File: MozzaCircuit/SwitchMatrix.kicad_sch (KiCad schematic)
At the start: 94 parts, among them SW13 SW_ChocV2_rev, SW14 SW_ChocV2_rev, SW15 SW_ChocV2_rev, SW21 SW_ChocV2_rev, SW22 SW_ChocV2_rev, SW23 SW_ChocV2_rev, SW24 SW_ChocV2_rev, SW25 SW_ChocV2_rev, SW31 SW_ChocV2_rev, SW32 SW_ChocV2_rev, SW33 SW_ChocV2_rev, SW34 SW_ChocV2_rev, SW35 SW_ChocV2_rev, SW41 SW_ChocV2_rev, SW42 SW_ChocV2_rev, SW43 SW_ChocV2_rev, SW44 SW_ChocV2_rev, SW51 SW_ChocV2_rev, SW52 SW_ChocV2_rev, SW53 SW_ChocV2_rev, SW54 SW_ChocV2_rev, SW61 SW_ChocV2_rev, SW62 SW_ChocV2_rev, SW63 SW_ChocV2_rev, SW64 SW_ChocV2_rev, SW71 SW_ChocV2_rev, SW72 SW_ChocV2_rev, SW73 SW_ChocV2_rev, SW82 SW_ChocV2_rev, SW83 SW_ChocV2_rev, SW84 SW_ChocV2_rev

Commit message: led right ends wiring
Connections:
- net 5VD: now also SW25.4; no longer SW25.5
- net GNDD: now also SW25.5; no longer SW25.4
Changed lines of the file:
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@@
   (junction (at 160.02 91.44) (diameter 0) (color 0 0 0 0)
   )
+  (junction (at 72.39 138.43) (diameter 0) (color 0 0 0 0)
+  )
   (junction (at 50.8 76.2) (diameter 0) (color 0 0 0 0)
   )
@@
   (junction (at 234.95 138.43) (diameter 0) (color 0 0 0 0)
   )
+  (junction (at 72.39 130.81) (diameter 0) (color 0 0 0 0)
+  )
   (junction (at 129.54 113.03) (diameter 0) (color 0 0 0 0)
   )
@@
   (junction (at 91.44 80.01) (diameter 0) (color 0 0 0 0)
   )
+  (junction (at 53.34 130.81) (diameter 0) (color 0 0 0 0)
+  )
   (junction (at 88.9 160.02) (diameter 0) (color 0 0 0 0)
   )
@@
   (junction (at 64.77 116.84) (diameter 0) (color 0 0 0 0)
   )
+  (junction (at 53.34 138.43) (diameter 0) (color 0 0 0 0)
+  )
   (junction (at 146.05 160.02) (diameter 0) (color 0 0 0 0)
   )
@@
     (stroke (width 0) (type default) (color 0 0 0 0))
   )
+  (wire (pts (xy 34.29 130.81) (xy 53.34 130.81))
+    (stroke (width 0) (type default) (color 0 0 0 0))
+  )
   (wire (pts (xy 110.49 80.01) (xy 129.54 80.01))
     (stroke (width 0) (type default) (color 0 0 0 0))
@@
     (stroke (width 0) (type default) (color 0 0 0 0))
   )
+  (wire (pts (xy 34.29 138.43) (xy 53.34 138.43))
+    (stroke (width 0) (type default) (color 0 0 0 0))
+  )
   (wire (pts (xy 165.1 154.94) (xy 184.15 154.94))
     (stroke (width 0) (type default) (color 0 0 0 0))
@@
     (stroke (width 0) (type default) (color 0 0 0 0))
   )
+  (wire (pts (xy 53.34 138.43) (xy 72.39 138.43))
+    (stroke (width 0) (type default) (color 0 0 0 0))
+  )
   (wire (pts (xy 53.34 105.41) (xy 72.39 105.41))
     (stroke (width 0) (type default) (color 0 0 0 0))
@@
   )
   (wire (pts (xy 72.39 138.43) (xy 184.15 138.43))
+    (stroke (width 0) (type default) (color 0 0 0 0))
+  )
+  (wire (pts (xy 53.34 130.81) (xy 72.39 130.81))
     (stroke (width 0) (type default) (color 0 0 0 0))
   )
@@
     )
   )
-  (global_label "5VD" (shape input) (at 53.34 138.43 0) (fields_autoplaced)
-    (effects (font (size 1.27 1.27)) (justify left))
-    (property "Intersheet References" "${INTERSHEET_REFS}" (id 0) (at 59.3212 138.3506 0)
-      (effects (font (size 1.27 1.27)) (justify left) hide)
-    )
-  )
   (global_label "COL7" (shape input) (at 146.05 167.64 270) (fields_autoplaced)
     (effects (font (size 1.27 1.27)) (justify right))
@@
     (effects (font (size 1.27 1.27)) (justify left))
     (property "Intersheet References" "${INTERSHEET_REFS}" (id 0) (at 191.8245 101.5206 0)
-      (effects (font (size 1.27 1.27)) (justify left) hide)
-    )
-  )
-  (global_label "5VD" (shape input) (at 34.29 130.81 0) (fields_autoplaced)
-    (effects (font (size 1.27 1.27)) (justify left))
-    (property "Intersheet References" "${INTERSHEET_REFS}" (id 0) (at 40.2712 130.7306 0)
       (effects (font (size 1.27 1.27)) (justify left) hide)
     )
@@
     (pin "2")
   )
-  (symbol (lib_id "power:GNDD") (at 53.34 130.81 90) (unit 1)
-    (in_bom yes) (on_board yes) (fields_autoplaced)
-    (property "Reference" "#PWR0138" (id 0) (at 59.69 130.81 0)
-      (effects (font (size 1.27 1.27)) hide)
-    )
-    (property "Value" "GNDD" (id 1) (at 57.15 130.8099 90)
-      (effects (font (size 1.27 1.27)) (justify right))
-    )
-    (property "Footprint" "" (id 2) (at 53.34 130.81 0)
-      (effects (font (size 1.27 1.27)) hide)
-    )
-    (property "Datasheet" "" (id 3) (at 53.34 130.81 0)
-      (effects (font (size 1.27 1.27)) hide)
-    )
-    (pin "1")
-  )
   (symbol (lib_id "Device:D_Small") (at 86.36 91.44 0) (unit 1)
     (in_bom yes) (on_board yes)
@@
     (pin "5")
   )
-  (symbol (lib_id "power:GNDD") (at 34.29 138.43 90) (unit 1)
-    (in_bom yes) (on_board yes) (fields_autoplaced)
-    (property "Reference" "#PWR0139" (id 0) (at 40.64 138.43 0)
-      (effects (font (size 1.27 1.27)) hide)
-    )
-    (property "Value" "GNDD" (id 1) (at 38.1 138.4299 90)
-      (effects (font (size 1.27 1.27)) (justify right))
-    )
-    (property "Footprint" "" (id 2) (at 34.29 138.43 0)
-      (effects (font (size 1.27 1.27)) hide)
-    )
-    (property "Datasheet" "" (id 3) (at 34.29 138.43 0)
-      (effects (font (size 1.27 1.27)) hide)
-    )
-    (pin "1")
-  )
   (symbol (lib_name "SW_ChocV2_rev_12") (lib_id "00_KeyParts:SW_ChocV2_rev") (at 69.85 83.82 90) (mirror x) (unit 1)

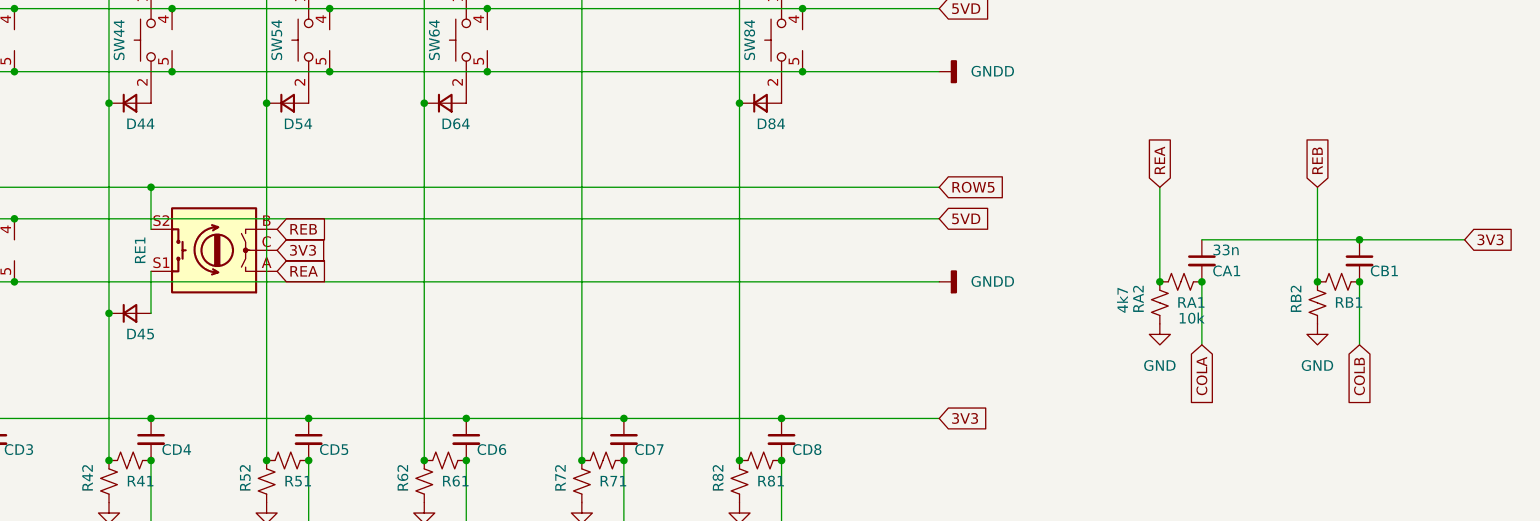
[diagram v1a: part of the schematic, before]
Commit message: rotend debounce
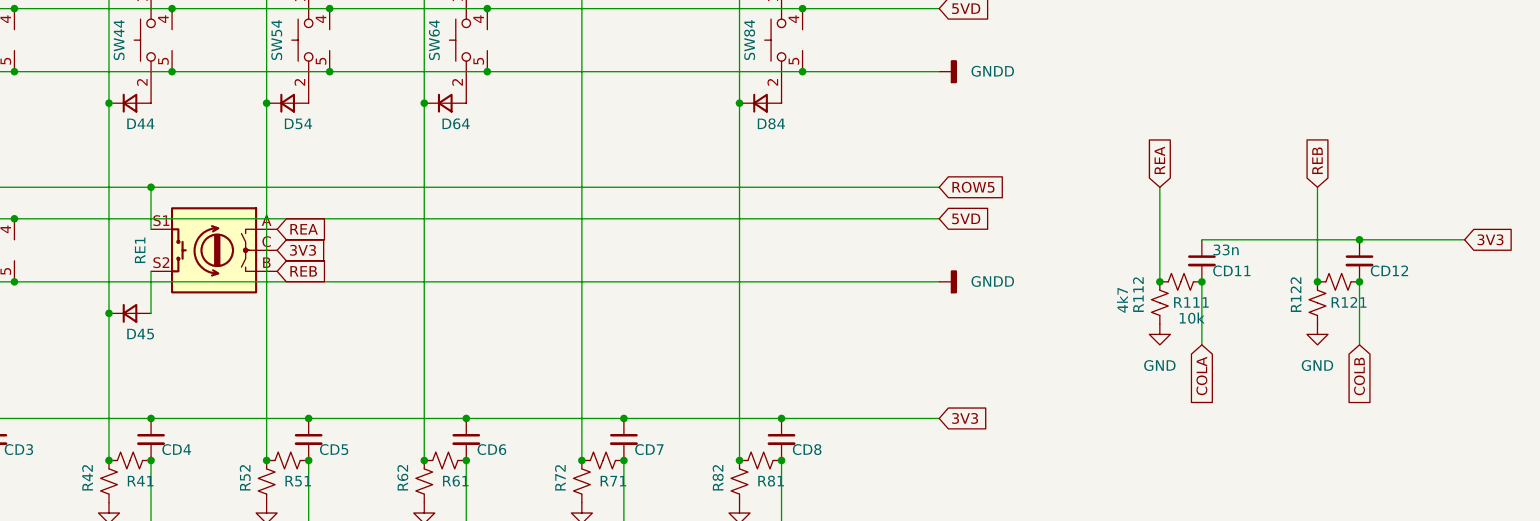
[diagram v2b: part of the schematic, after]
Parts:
- renumbered CA1 to CD11, CB1 to CD12, RA1 to R111, RA2 to R112, RB1 to R121, RB2 to R122
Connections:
- net ROW5: now also RE1.S1; no longer RE1.S2
- net at D45.2 (A): now also RE1.S2; no longer RE1.S1
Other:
- moved on the sheet: RE1
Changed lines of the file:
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@@
     )
   )
-  (global_label "REA" (shape input) (at 104.14 137.16 0) (fields_autoplaced)
+  (global_label "REA" (shape input) (at 104.14 132.08 0) (fields_autoplaced)
     (effects (font (size 1.27 1.27)) (justify left))
-    (property "Intersheet References" "${INTERSHEET_REFS}" (id 0) (at 110.0607 137.0806 0)
+    (property "Intersheet References" "${INTERSHEET_REFS}" (id 0) (at 110.0607 132.0006 0)
       (effects (font (size 1.27 1.27)) (justify left) hide)
     )
@@
     )
   )
-  (global_label "REB" (shape input) (at 104.14 132.08 0) (fields_autoplaced)
+  (global_label "REB" (shape input) (at 104.14 137.16 0) (fields_autoplaced)
     (effects (font (size 1.27 1.27)) (justify left))
-    (property "Intersheet References" "${INTERSHEET_REFS}" (id 0) (at 110.2421 132.0006 0)
+    (property "Intersheet References" "${INTERSHEET_REFS}" (id 0) (at 110.2421 137.0806 0)
       (effects (font (size 1.27 1.27)) (justify left) hide)
     )
@@
   (symbol (lib_id "Device:C_Small") (at 215.9 135.89 0) (unit 1)
     (in_bom yes) (on_board yes)
-    (property "Reference" "CA1" (id 0) (at 217.17 137.16 0)
+    (property "Reference" "CD11" (id 0) (at 217.17 137.16 0)
       (effects (font (size 1.27 1.27)) (justify left))
     )
@@
   (symbol (lib_id "Device:R_Small_US") (at 232.41 138.43 90) (unit 1)
     (in_bom yes) (on_board yes)
-    (property "Reference" "RB1" (id 0) (at 233.68 140.97 90))
+    (property "Reference" "R121" (id 0) (at 233.68 140.97 90))
     (property "Value" "R_Small_US" (id 1) (at 232.41 134.62 90)
       (effects (font (size 1.27 1.27)) hide)
@@
   (symbol (lib_id "Device:R_Small_US") (at 210.82 140.97 0) (unit 1)
     (in_bom yes) (on_board yes)
-    (property "Reference" "RA2" (id 0) (at 208.28 142.24 90)
+    (property "Reference" "R112" (id 0) (at 208.28 142.24 90)
       (effects (font (size 1.27 1.27)) (justify left))
     )
@@
     (pin "1")
   )
-  (symbol (lib_id "Device:RotaryEncoder_Switch") (at 96.52 134.62 180) (unit 1)
+  (symbol (lib_id "Device:RotaryEncoder_Switch") (at 96.52 134.62 0) (mirror y) (unit 1)
     (in_bom yes) (on_board yes)
     (property "Reference" "RE1" (id 0) (at 87.63 134.62 90))
-    (property "Value" "RotaryEncoder_Switch" (id 1) (at 96.52 142.24 0)
-      (effects (font (size 1.27 1.27)) hide)
-    )
-    (property "Footprint" "00_KeyParts:RotaryEncoder_Bourns_PEC12R-4215F" (id 2) (at 100.33 138.684 0)
-      (effects (font (size 1.27 1.27)) hide)
-    )
-    (property "Datasheet" "~" (id 3) (at 96.52 141.224 0)
+    (property "Value" "RotaryEncoder_Switch" (id 1) (at 96.52 127 0)
+      (effects (font (size 1.27 1.27)) hide)
+    )
+    (property "Footprint" "00_KeyParts:RotaryEncoder_Bourns_PEC12R-4215F" (id 2) (at 100.33 130.556 0)
+      (effects (font (size 1.27 1.27)) hide)
+    )
+    (property "Datasheet" "~" (id 3) (at 96.52 128.016 0)
       (effects (font (size 1.27 1.27)) hide)
     )
@@
   (symbol (lib_id "Device:R_Small_US") (at 213.36 138.43 90) (unit 1)
     (in_bom yes) (on_board yes)
-    (property "Reference" "RA1" (id 0) (at 214.63 140.97 90))
+    (property "Reference" "R111" (id 0) (at 214.63 140.97 90))
     (property "Value" "10k" (id 1) (at 214.63 142.875 90))
     (property "Footprint" "00_KeyParts:R_1608_HandSolder_both_sides" (id 2) (at 213.36 138.43 0)
@@
   (symbol (lib_id "Device:C_Small") (at 234.95 135.89 0) (unit 1)
     (in_bom yes) (on_board yes)
-    (property "Reference" "CB1" (id 0) (at 236.22 137.16 0)
+    (property "Reference" "CD12" (id 0) (at 236.22 137.16 0)
       (effects (font (size 1.27 1.27)) (justify left))
     )
@@
   (symbol (lib_id "Device:R_Small_US") (at 229.87 140.97 0) (unit 1)
     (in_bom yes) (on_board yes)
-    (property "Reference" "RB2" (id 0) (at 227.33 142.24 90)
-      (effects (font (size 1.27 1.27)) (justify left))
-    )
+    (property "Reference" "R122" (id 0) (at 227.33 142.24 90)
+      (effects (font (size 1.27 1.27)) (justify left))
+    )
